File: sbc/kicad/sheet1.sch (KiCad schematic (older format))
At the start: 35 parts, among them J1 AC/DC IN, J2 5V IN, U1 LM7805, U2 74LS00, U3 74LS04

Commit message: Minor updates.
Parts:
- added J12: REG. POWER, Connector_PinHeader_2.54mm:PinHeader_1x02_P2.54mm_Vertical, symbol Connector_Generic:Conn_01x02
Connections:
- net VCC: now also J12.1 (Pin_1); no longer C3.1, U1.3 (VO)
- new net: C3.1, J12.2 (Pin_2), U1.3 (VO)
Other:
- note added: "POWER (OPTIONAL)"
- note removed: "POWER"
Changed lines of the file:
@@
 Sheet 2 6
 Title "6800 SIngle Board Computer"
-Date "2022-02-06"
+Date "2022-02-07"
 Rev "0.1"
 Comp "Jeff Tranter"
@@
 L power:VCC #PWR04
 U 1 1 61E4A38D
-P 6750 2100
-F 0 "#PWR04" H 6750 1950 50  0001 C CNN
-F 1 "VCC" H 6767 2273 50  0000 C CNN
-F 2 "" H 6750 2100 50  0001 C CNN
-F 3 "" H 6750 2100 50  0001 C CNN
-	1    6750 2100
-	1    0    0    -1
+P 6850 2100
+F 0 "#PWR04" H 6850 1950 50  0001 C CNN
+F 1 "VCC" V 6867 2273 50  0000 C CNN
+F 2 "" H 6850 2100 50  0001 C CNN
+F 3 "" H 6850 2100 50  0001 C CNN
+	1    6850 2100
+	0    1    1    0
 $EndComp
 Wire Wire Line
@@
 Text Notes 1900 2350 0    79   ~ 0
 UNREGULATED\nAC OR DC IN\n7-15V
-Text Notes 5050 1450 0    118  ~ 0
-POWER
+Text Notes 4500 1450 0    118  ~ 0
+POWER (OPTIONAL)
 $Comp
 L Diode:1N4001 D2
@@
 	4900 1750 6750 1750
 Connection ~ 4900 1750
+$Comp
+L Connector_Generic:Conn_01x02 J12
+U 1 1 6201E14B
+P 6850 1900
+F 0 "J12" V 6850 1650 50  0000 C CNN
+F 1 "REG. POWER" V 6850 2200 50  0000 C CNN
+F 2 "Connector_PinHeader_2.54mm:PinHeader_1x02_P2.54mm_Vertical" H 6850 1900 50  0001 C CNN
+F 3 "~" H 6850 1900 50  0001 C CNN
+	1    6850 1900
+	0    1    -1   0
+$EndComp
+$Comp
+L power:PWR_FLAG #FLG0101
+U 1 1 62045FE8
+P 6850 2700
+F 0 "#FLG0101" H 6850 2775 50  0001 C CNN
+F 1 "PWR_FLAG" H 6850 2873 50  0000 C CNN
+F 2 "" H 6850 2700 50  0001 C CNN
+F 3 "~" H 6850 2700 50  0001 C CNN
+	1    6850 2700
+	-1   0    0    1
+$EndComp
+Wire Wire Line
+	6850 2100 6850 2700
+Connection ~ 6850 2100
 $EndSCHEMATC

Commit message: Various updates.
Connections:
- net GND: now also U2.10, U2.12, U2.13, U2.9, U3.13
- no-connect marks 8 -> 3
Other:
- note added: "REGULATED\n5V IN SELECT"
- note added: "UNREGULATED\nPOWER SELECT"
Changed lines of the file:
@@
 Sheet 2 6
 Title "6800 SIngle Board Computer"
-Date "2022-02-07"
+Date "2022-02-09"
 Rev "0.1"
 Comp "Jeff Tranter"
@@
 	1    0    0    -1
 $EndComp
-NoConn ~ 6250 5000
 NoConn ~ 6850 5000
-NoConn ~ 6250 4450
-NoConn ~ 6250 4250
 NoConn ~ 6850 4350
-NoConn ~ 7250 4250
-NoConn ~ 7250 4450
 NoConn ~ 7850 4350
 Text Notes 1900 2350 0    79   ~ 0
@@
 	6850 2100 6850 2700
 Connection ~ 6850 2100
+Text Notes 1450 4300 0    50   ~ 0
+REGULATED\n5V IN SELECT
+Text Notes 6200 1700 0    50   ~ 0
+UNREGULATED\nPOWER SELECT
+$Comp
+L power:GND #PWR0101
+U 1 1 62049965
+P 6250 5100
+F 0 "#PWR0101" H 6250 4850 50  0001 C CNN
+F 1 "GND" H 6255 4927 50  0000 C CNN
+F 2 "" H 6250 5100 50  0001 C CNN
+F 3 "" H 6250 5100 50  0001 C CNN
+	1    6250 5100
+	1    0    0    -1
+$EndComp
+$Comp
+L power:GND #PWR0102
+U 1 1 6204A1DA
+P 6250 4550
+F 0 "#PWR0102" H 6250 4300 50  0001 C CNN
+F 1 "GND" H 6255 4377 50  0000 C CNN
+F 2 "" H 6250 4550 50  0001 C CNN
+F 3 "" H 6250 4550 50  0001 C CNN
+	1    6250 4550
+	1    0    0    -1
+$EndComp
+$Comp
+L power:GND #PWR0103
+U 1 1 6204A7F3
+P 7250 4550
+F 0 "#PWR0103" H 7250 4300 50  0001 C CNN
+F 1 "GND" H 7255 4377 50  0000 C CNN
+F 2 "" H 7250 4550 50  0001 C CNN
+F 3 "" H 7250 4550 50  0001 C CNN
+	1    7250 4550
+	1    0    0    -1
+$EndComp
+Wire Wire Line
+	7250 4250 7250 4450
+Wire Wire Line
+	7250 4450 7250 4550
+Connection ~ 7250 4450
+Wire Wire Line
+	6250 4250 6250 4450
+Wire Wire Line
+	6250 4450 6250 4550
+Connection ~ 6250 4450
+Wire Wire Line
+	6250 5000 6250 5100
 $EndSCHEMATC

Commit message: Getting close to ready to order PCBs. Check in all files.
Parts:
- added unit 5 of U2
- added unit 7 of U3
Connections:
- net GND: now also U2.7 (GND), U3.7 (GND)
- net VCC: now also U2.14 (VCC), U3.14 (VCC)
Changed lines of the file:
@@
 Sheet 2 6
 Title "6800 SIngle Board Computer"
-Date "2022-02-09"
+Date "2022-02-12"
 Rev "0.1"
 Comp "Jeff Tranter"
@@
 Wire Wire Line
 	6250 5000 6250 5100
+$Comp
+L 74xx:74LS00 U2
+U 5 1 620849AD
+P 8600 5300
+F 0 "U2" H 8450 5650 50  0000 C CNN
+F 1 "74LS00" H 8750 5650 50  0000 C CNN
+F 2 "Package_DIP:DIP-14_W7.62mm_Socket" H 8600 5300 50  0001 C CNN
+F 3 "http://www.ti.com/lit/gpn/sn74ls00" H 8600 5300 50  0001 C CNN
+	5    8600 5300
+	1    0    0    -1
+$EndComp
+$Comp
+L 74xx:74LS04 U3
+U 7 1 62087D0F
+P 7900 5300
+F 0 "U3" H 7750 5650 50  0000 C CNN
+F 1 "74LS04" H 8050 5650 50  0000 C CNN
+F 2 "Package_DIP:DIP-14_W7.62mm_Socket" H 7900 5300 50  0001 C CNN
+F 3 "http://www.ti.com/lit/gpn/sn74LS04" H 7900 5300 50  0001 C CNN
+	7    7900 5300
+	1    0    0    -1
+$EndComp
+$Comp
+L power:GND #PWR081
+U 1 1 6209947A
+P 7900 5800
+F 0 "#PWR081" H 7900 5550 50  0001 C CNN
+F 1 "GND" H 7905 5627 50  0000 C CNN
+F 2 "" H 7900 5800 50  0001 C CNN
+F 3 "" H 7900 5800 50  0001 C CNN
+	1    7900 5800
+	1    0    0    -1
+$EndComp
+$Comp
+L power:GND #PWR082
+U 1 1 62099D08
+P 8600 5800
+F 0 "#PWR082" H 8600 5550 50  0001 C CNN
+F 1 "GND" H 8605 5627 50  0000 C CNN
+F 2 "" H 8600 5800 50  0001 C CNN
+F 3 "" H 8600 5800 50  0001 C CNN
+	1    8600 5800
+	1    0    0    -1
+$EndComp
+$Comp
+L power:VCC #PWR079
+U 1 1 6209A4EC
+P 7900 4800
+F 0 "#PWR079" H 7900 4650 50  0001 C CNN
+F 1 "VCC" H 7917 4973 50  0000 C CNN
+F 2 "" H 7900 4800 50  0001 C CNN
+F 3 "" H 7900 4800 50  0001 C CNN
+	1    7900 4800
+	1    0    0    -1
+$EndComp
+$Comp
+L power:VCC #PWR080
+U 1 1 6209AE4E
+P 8600 4800
+F 0 "#PWR080" H 8600 4650 50  0001 C CNN
+F 1 "VCC" H 8617 4973 50  0000 C CNN
+F 2 "" H 8600 4800 50  0001 C CNN
+F 3 "" H 8600 4800 50  0001 C CNN
+	1    8600 4800
+	1    0    0    -1
+$EndComp
 $EndSCHEMATC

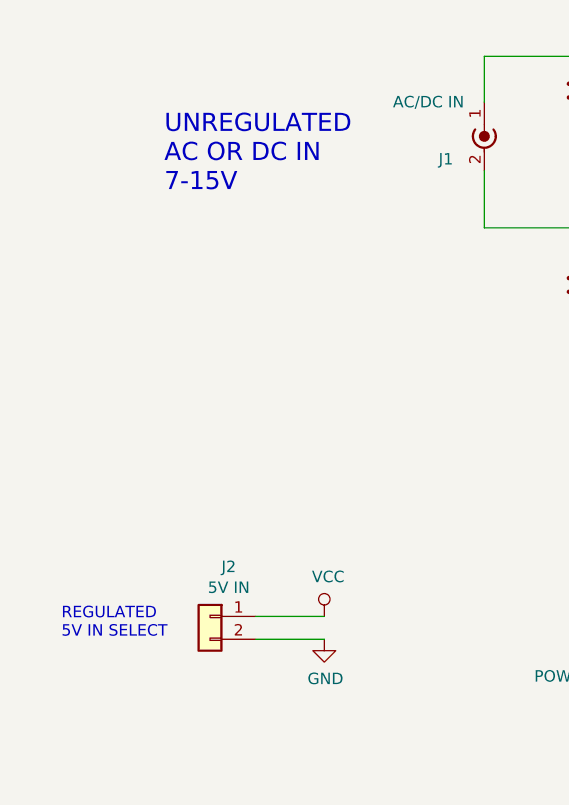
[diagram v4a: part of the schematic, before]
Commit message: Some corrections to schematic and added to documentation.
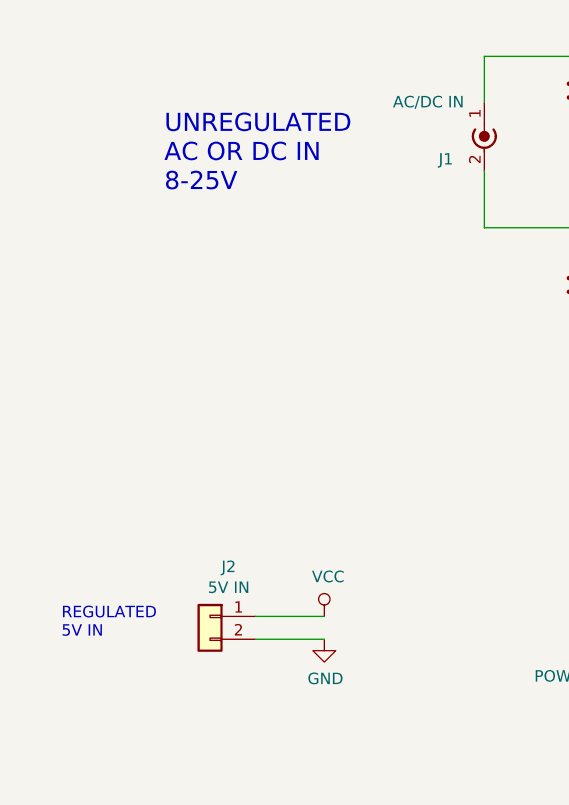
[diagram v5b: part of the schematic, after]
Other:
- note added: "REGULATED\n5V IN"
- note added: "UNREGULATED\nAC OR DC IN\n8-25V"
- note removed: "REGULATED\n5V IN SELECT"
- note removed: "UNREGULATED\nAC OR DC IN\n7-15V"
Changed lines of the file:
@@
 Sheet 2 6
 Title "6800 SIngle Board Computer"
-Date "2022-02-12"
+Date "2022-03-02"
 Rev "0.1"
 Comp "Jeff Tranter"
@@
 NoConn ~ 7850 4350
 Text Notes 1900 2350 0    79   ~ 0
-UNREGULATED\nAC OR DC IN\n7-15V
+UNREGULATED\nAC OR DC IN\n8-25V
 Text Notes 4500 1450 0    118  ~ 0
 POWER (OPTIONAL)
@@
 Connection ~ 6850 2100
 Text Notes 1450 4300 0    50   ~ 0
-REGULATED\n5V IN SELECT
+REGULATED\n5V IN
 Text Notes 6200 1700 0    50   ~ 0
 UNREGULATED\nPOWER SELECT

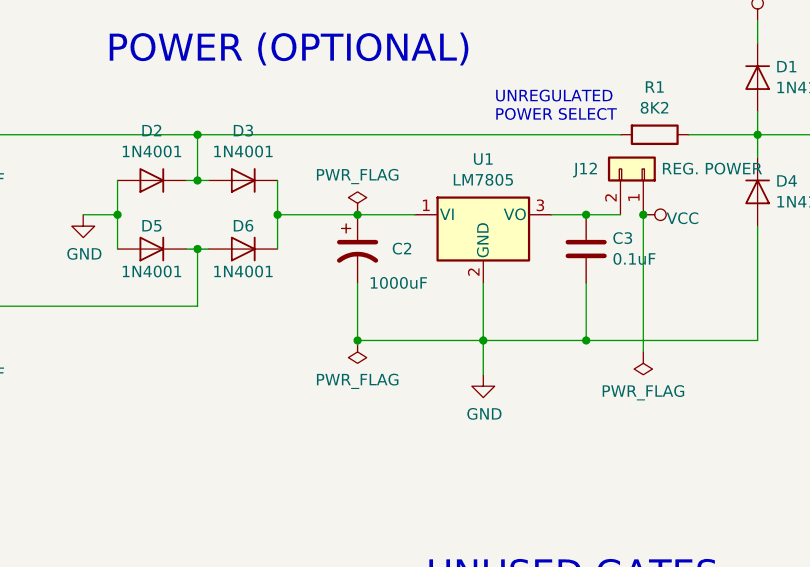
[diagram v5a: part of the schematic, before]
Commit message: Change C2 to 100uF.
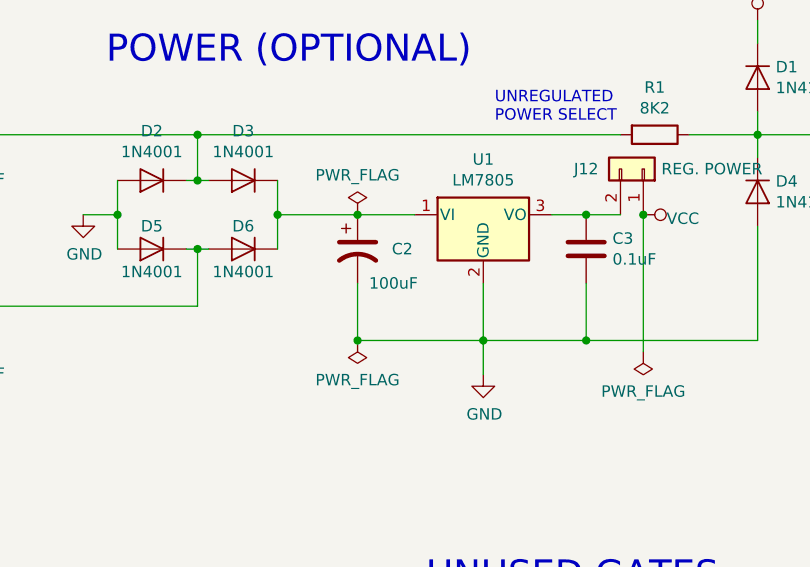
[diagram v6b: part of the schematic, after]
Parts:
- C2: value 1000uF -> 100uF
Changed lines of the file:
@@
 P 5600 2250
 F 0 "C2" H 5750 2250 50  0000 L CNN
-F 1 "1000uF" H 5650 2100 50  0000 L CNN
+F 1 "100uF" H 5650 2100 50  0000 L CNN
 F 2 "Capacitor_THT:CP_Radial_D5.0mm_P2.00mm" H 5600 2250 50  0001 C CNN
 F 3 "~" H 5600 2250 50  0001 C CNN
